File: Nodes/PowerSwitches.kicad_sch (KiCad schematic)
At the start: 46 parts, among them IC1 VNQ9080AJTR, IC2 VNQ9080AJTR, T21 Conn_01x01, T22 Conn_01x01

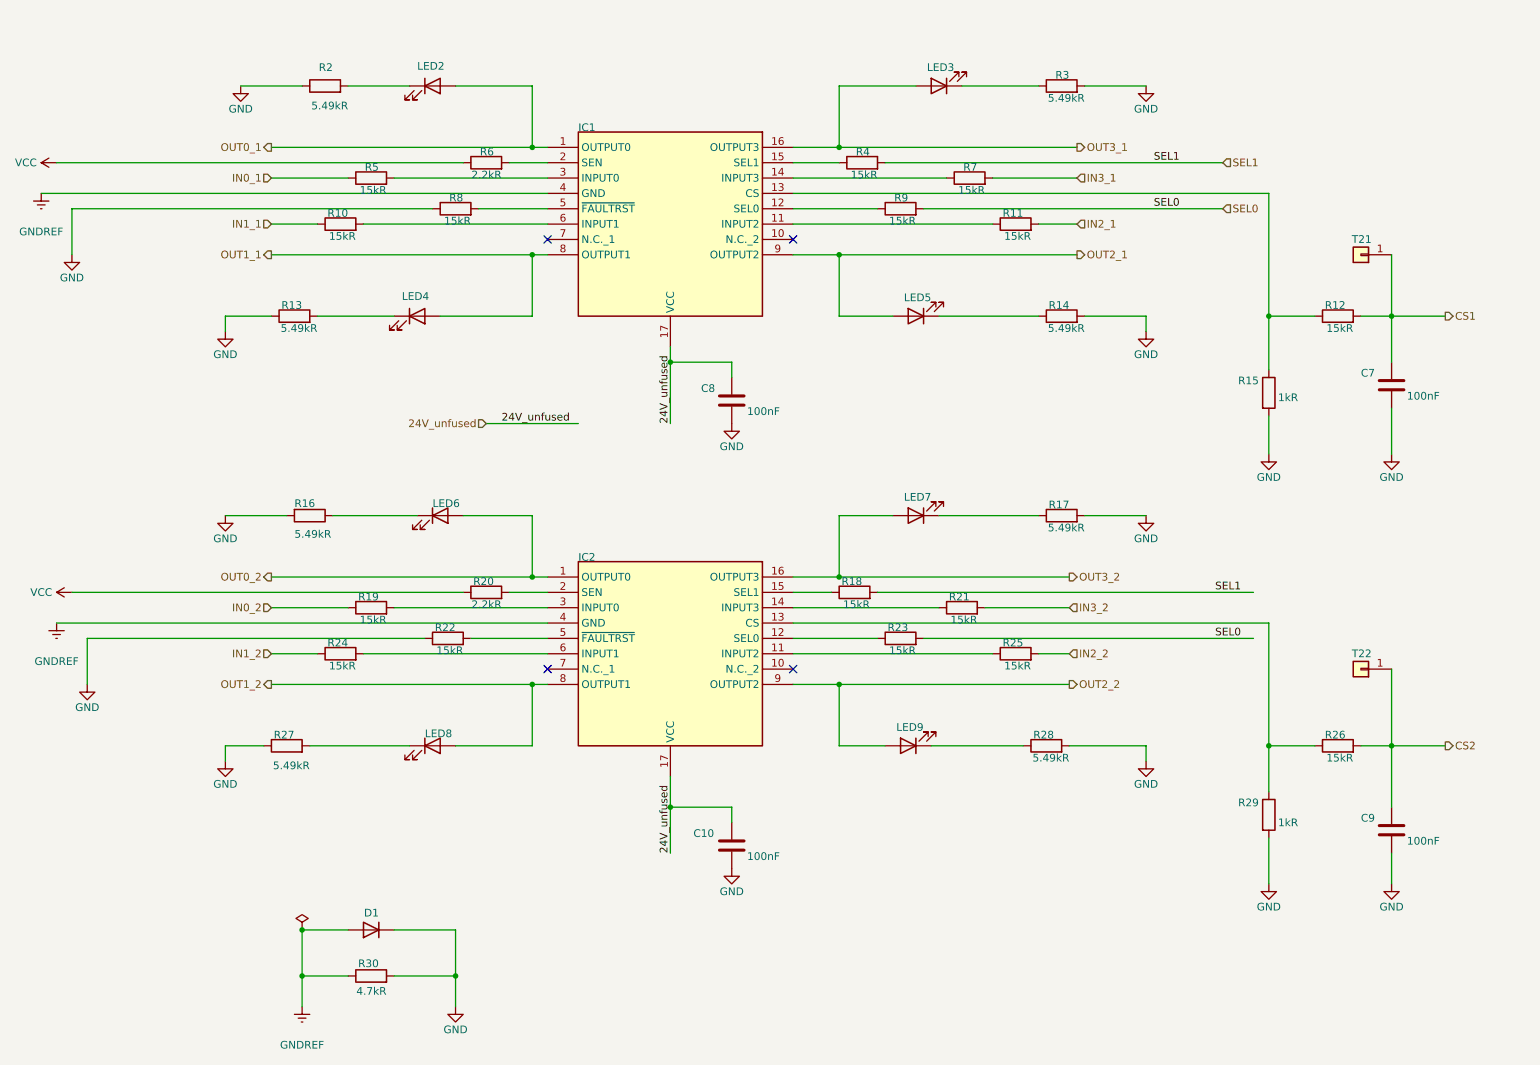
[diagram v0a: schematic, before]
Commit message: Nodes v2.1.2 Improved
- Improved schematic design
- Added two 4.7 uF caps according to the datasheets of the microchips
- Other small changes
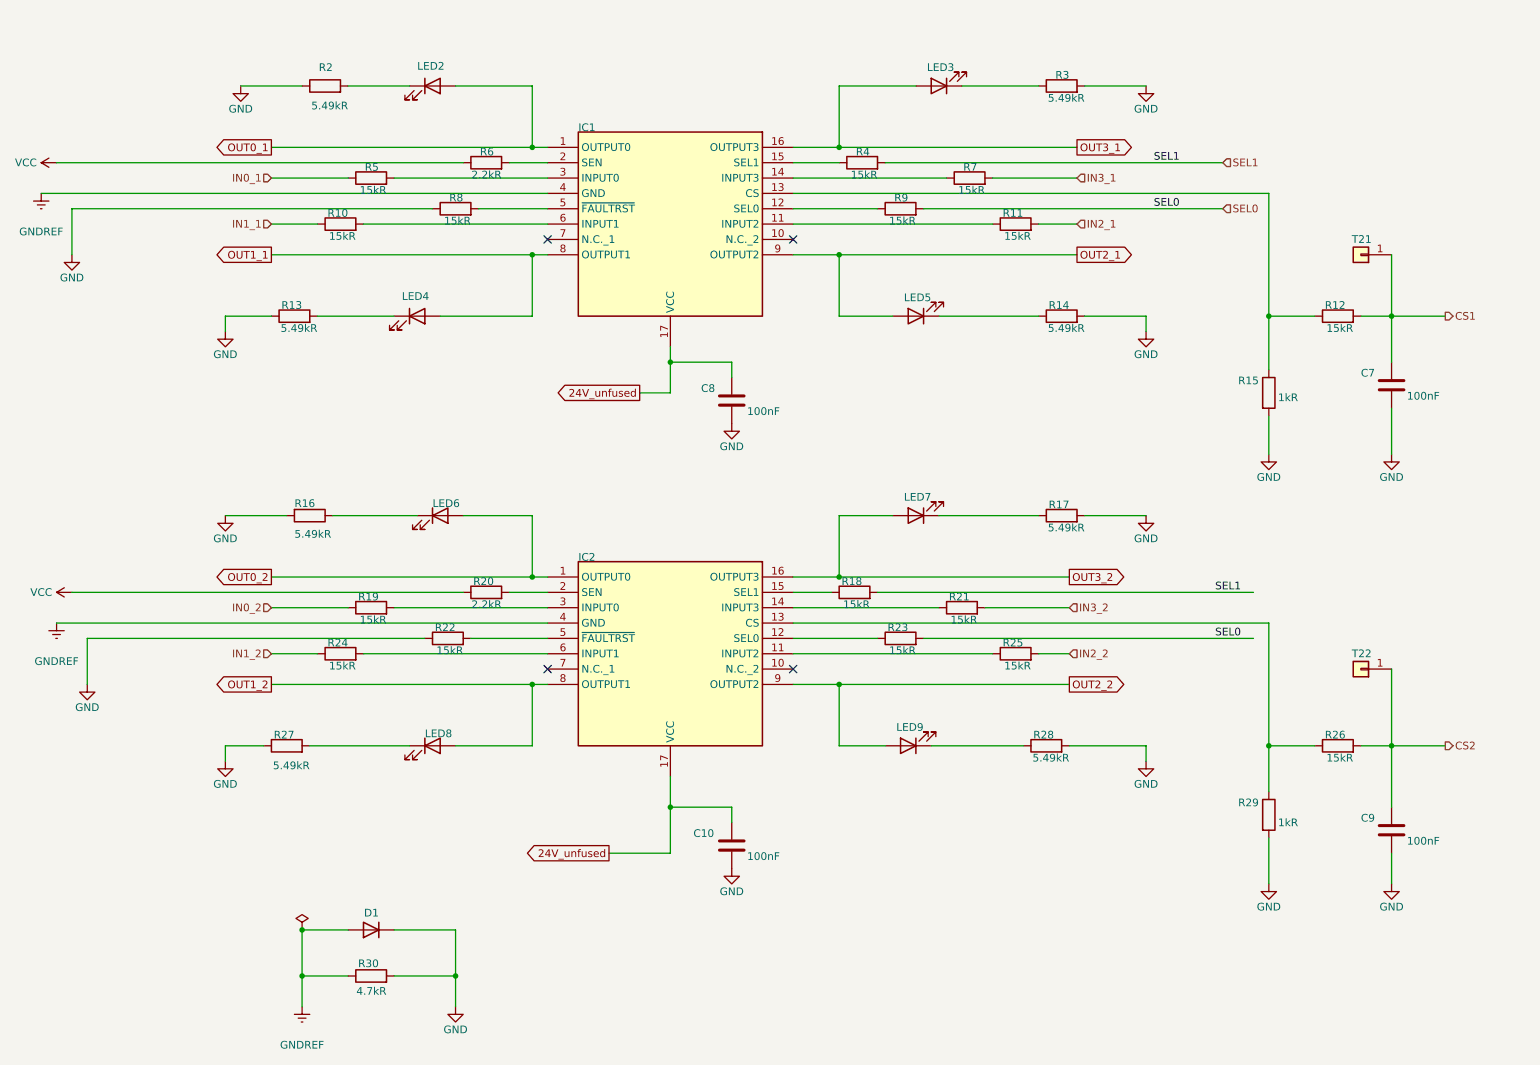
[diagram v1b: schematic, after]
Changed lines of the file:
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@@
+	(wire
+		(pts
+			(xy 125.73 77.47) (xy 120.65 77.47)
+		)
+		(stroke
+			(width 0.254)
+			(type default)
+		)
+	)
 	(wire
 		(pts
@@
 	(wire
 		(pts
-			(xy 125.73 72.39) (xy 125.73 82.55)
-		)
-		(stroke
-			(width 0.254)
-			(type default)
-		)
-	)
-	(wire
-		(pts
 			(xy 146.05 125.73) (xy 153.67 125.73)
 		)
@@
 	(wire
 		(pts
+			(xy 115.57 153.67) (xy 125.73 153.67)
+		)
+		(stroke
+			(width 0.254)
+			(type default)
+		)
+	)
+	(wire
+		(pts
 			(xy 102.87 64.77) (xy 102.87 54.61)
 		)
@@
 	(wire
 		(pts
-			(xy 95.25 82.55) (xy 110.49 82.55)
-		)
-		(stroke
-			(width 0.254)
-			(type default)
-		)
-	)
-	(wire
-		(pts
 			(xy 224.79 135.89) (xy 224.79 143.51)
 		)
@@
 		(pts
 			(xy 224.79 44.45) (xy 224.79 64.77)
+		)
+		(stroke
+			(width 0.254)
+			(type default)
+		)
+	)
+	(wire
+		(pts
+			(xy 125.73 72.39) (xy 125.73 77.47)
 		)
 		(stroke
@@
 		)
 	)
-	(label "24V_unfused"
-		(at 97.79 82.55 0)
-		(fields_autoplaced yes)
-		(effects
-			(font
-				(size 1.27 1.27)
-			)
-			(justify left bottom)
-		)
-	)
 	(label "SEL0"
 		(at 205.74 46.99 0)
@@
 		)
 	)
-	(label "24V_unfused"
-		(at 125.73 153.67 90)
-		(fields_autoplaced yes)
-		(effects
-			(font
-				(size 1.27 1.27)
-			)
-			(justify left bottom)
-		)
-	)
-	(label "24V_unfused"
-		(at 125.73 82.55 90)
-		(fields_autoplaced yes)
-		(effects
-			(font
-				(size 1.27 1.27)
-			)
-			(justify left bottom)
-		)
-	)
 	(label "SEL1"
 		(at 215.9 110.49 0)
@@
 		)
 	)
+	(global_label "OUT2_2"
+		(shape output)
+		(at 191.77 125.73 0)
+		(fields_autoplaced yes)
+		(effects
+			(font
+				(size 1.27 1.27)
+			)
+			(justify left)
+		)
+		(property "Intersheetrefs" "${INTERSHEET_REFS}"
+			(at 201.7704 125.73 0)
+			(effects
+				(font
+					(size 1.27 1.27)
+				)
+				(justify left)
+				(hide yes)
+			)
+		)
+	)
+	(global_label "OUT3_1"
+		(shape output)
+		(at 193.04 36.83 0)
+		(fields_autoplaced yes)
+		(effects
+			(font
+				(size 1.27 1.27)
+			)
+			(justify left)
+		)
+		(property "Intersheetrefs" "${INTERSHEET_REFS}"
+			(at 203.0404 36.83 0)
+			(effects
+				(font
+					(size 1.27 1.27)
+				)
+				(justify left)
+				(hide yes)
+			)
+		)
+	)
+	(global_label "OUT1_1"
+		(shape output)
+		(at 59.69 54.61 180)
+		(fields_autoplaced yes)
+		(effects
+			(font
+				(size 1.27 1.27)
+			)
+			(justify right)
+		)
+		(property "Intersheetrefs" "${INTERSHEET_REFS}"
+			(at 49.6896 54.61 0)
+			(effects
+				(font
+					(size 1.27 1.27)
+				)
+				(justify right)
+				(hide yes)
+			)
+		)
+	)
+	(global_label "OUT0_1"
+		(shape output)
+		(at 59.69 36.83 180)
+		(fields_autoplaced yes)
+		(effects
+			(font
+				(size 1.27 1.27)
+			)
+			(justify right)
+		)
+		(property "Intersheetrefs" "${INTERSHEET_REFS}"
+			(at 49.6896 36.83 0)
+			(effects
+				(font
+					(size 1.27 1.27)
+				)
+				(justify right)
+				(hide yes)
+			)
+		)
+	)
+	(global_label "OUT1_2"
+		(shape output)
+		(at 59.69 125.73 180)
+		(fields_autoplaced yes)
+		(effects
+			(font
+				(size 1.27 1.27)
+			)
+			(justify right)
+		)
+		(property "Intersheetrefs" "${INTERSHEET_REFS}"
+			(at 49.6896 125.73 0)
+			(effects
+				(font
+					(size 1.27 1.27)
+				)
+				(justify right)
+				(hide yes)
+			)
+		)
+	)
+	(global_label "24V_unfused"
+		(shape output)
+		(at 115.57 153.67 180)
+		(fields_autoplaced yes)
+		(effects
+			(font
+				(size 1.27 1.27)
+			)
+			(justify right)
+		)
+		(property "Intersheetrefs" "${INTERSHEET_REFS}"
+			(at 100.6712 153.67 0)
+			(effects
+				(font
+					(size 1.27 1.27)
+				)
+				(justify right)
+				(hide yes)
+			)
+		)
+	)
+	(global_label "OUT2_1"
+		(shape output)
+		(at 193.04 54.61 0)
+		(fields_autoplaced yes)
+		(effects
+			(font
+				(size 1.27 1.27)
+			)
+			(justify left)
+		)
+		(property "Intersheetrefs" "${INTERSHEET_REFS}"
+			(at 203.0404 54.61 0)
+			(effects
+				(font
+					(size 1.27 1.27)
+				)
+				(justify left)
+				(hide yes)
+			)
+		)
+	)
+	(global_label "24V_unfused"
+		(shape output)
+		(at 120.65 77.47 180)
+		(fields_autoplaced yes)
+		(effects
+			(font
+				(size 1.27 1.27)
+			)
+			(justify right)
+		)
+		(property "Intersheetrefs" "${INTERSHEET_REFS}"
+			(at 105.7512 77.47 0)
+			(effects
+				(font
+					(size 1.27 1.27)
+				)
+				(justify right)
+				(hide yes)
+			)
+		)
+	)
+	(global_label "OUT0_2"
+		(shape output)
+		(at 59.69 107.95 180)
+		(fields_autoplaced yes)
+		(effects
+			(font
+				(size 1.27 1.27)
+			)
+			(justify right)
+		)
+		(property "Intersheetrefs" "${INTERSHEET_REFS}"
+			(at 49.6896 107.95 0)
+			(effects
+				(font
+					(size 1.27 1.27)
+				)
+				(justify right)
+				(hide yes)
+			)
+		)
+	)
+	(global_label "OUT3_2"
+		(shape output)
+		(at 191.77 107.95 0)
+		(fields_autoplaced yes)
+		(effects
+			(font
+				(size 1.27 1.27)
+			)
+			(justify left)
+		)
+		(property "Intersheetrefs" "${INTERSHEET_REFS}"
+			(at 201.7704 107.95 0)
+			(effects
+				(font
+					(size 1.27 1.27)
+				)
+				(justify left)
+				(hide yes)
+			)
+		)
+	)
 	(hierarchical_label "SEL0"
 		(shape input)
@@
 		)
 	)
-	(hierarchical_label "OUT3_1"
-		(shape output)
-		(at 193.04 36.83 0)
-		(fields_autoplaced yes)
-		(effects
-			(font
-				(size 1.27 1.27)
-			)
-			(justify left)
-		)
-	)
 	(hierarchical_label "CS1"
 		(shape output)
@@
 		)
 	)
-	(hierarchical_label "OUT1_1"
-		(shape output)
-		(at 59.69 54.61 180)
-		(fields_autoplaced yes)
-		(effects
-			(font
-				(size 1.27 1.27)
-			)
-			(justify right)
-		)
-	)
 	(hierarchical_label "IN2_1"
 		(shape input)
@@
 		)
 	)
-	(hierarchical_label "OUT1_2"
-		(shape output)
-		(at 59.69 125.73 180)
-		(fields_autoplaced yes)
-		(effects
-			(font
-				(size 1.27 1.27)
-			)
-			(justify right)
-		)
-	)
 	(hierarchical_label "IN0_2"
 		(shape input)
@@
 		)
 	)
-	(hierarchical_label "OUT0_2"
-		(shape output)
-		(at 59.69 107.95 180)
-		(fields_autoplaced yes)
-		(effects
-			(font
-				(size 1.27 1.27)
-			)
-			(justify right)
-		)
-	)
-	(hierarchical_label "OUT2_1"
-		(shape output)
-		(at 193.04 54.61 0)
-		(fields_autoplaced yes)
-		(effects
-			(font
-				(size 1.27 1.27)
-			)
-			(justify left)
-		)
-	)
-	(hierarchical_label "24V_unfused"
-		(shape input)
-		(at 95.25 82.55 180)
-		(fields_autoplaced yes)
-		(effects
-			(font
-				(size 1.27 1.27)
-			)
-			(justify right)
-		)
-	)
-	(hierarchical_label "OUT2_2"
-		(shape output)
-		(at 191.77 125.73 0)
-		(fields_autoplaced yes)
-		(effects
-			(font
-				(size 1.27 1.27)
-			)
-			(justify left)
-		)
-	)
 	(hierarchical_label "IN1_2"
 		(shape input)
@@
 		)
 	)
-	(hierarchical_label "OUT0_1"
-		(shape output)
-		(at 59.69 36.83 180)
-		(fields_autoplaced yes)
-		(effects
-			(font
-				(size 1.27 1.27)
-			)
-			(justify right)
-		)
-	)
 	(hierarchical_label "IN0_1"
 		(shape input)
@@
 		(fields_autoplaced yes)
 		(effects
-			(font
-				(size 1.27 1.27)
-			)
-			(justify left)
-		)
-	)
-	(hierarchical_label "OUT3_2"
-		(shape output)
-		(at 191.77 107.95 0)
-		(fields_autoplaced yes)
-		(effects

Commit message: Nodes v2.2
- This version not compatible with BOB v.2.1.2 and older!
- Completely new layout design
- New power supply system with new voltage regulators
- New microchip STM32G431RBTx for the Analog Node
- New connection system (instead of 18 pin headers now 8 pin and pins were grouped by functions)
- Reduced size of the board by 5%
- Removed power switch for the Analog Node (because this functionality is now provided by a separate voltage regulator. for a more stable voltage)
- Removable ground from the holes added
- Layer numbers added
- Small improvements of the components information were made
- New oscillator for the Nodes
- Removed CAN1, so now only one CAN connection due to the capabilities of the new microchip
- Other small changes and fixes on the schematic and design
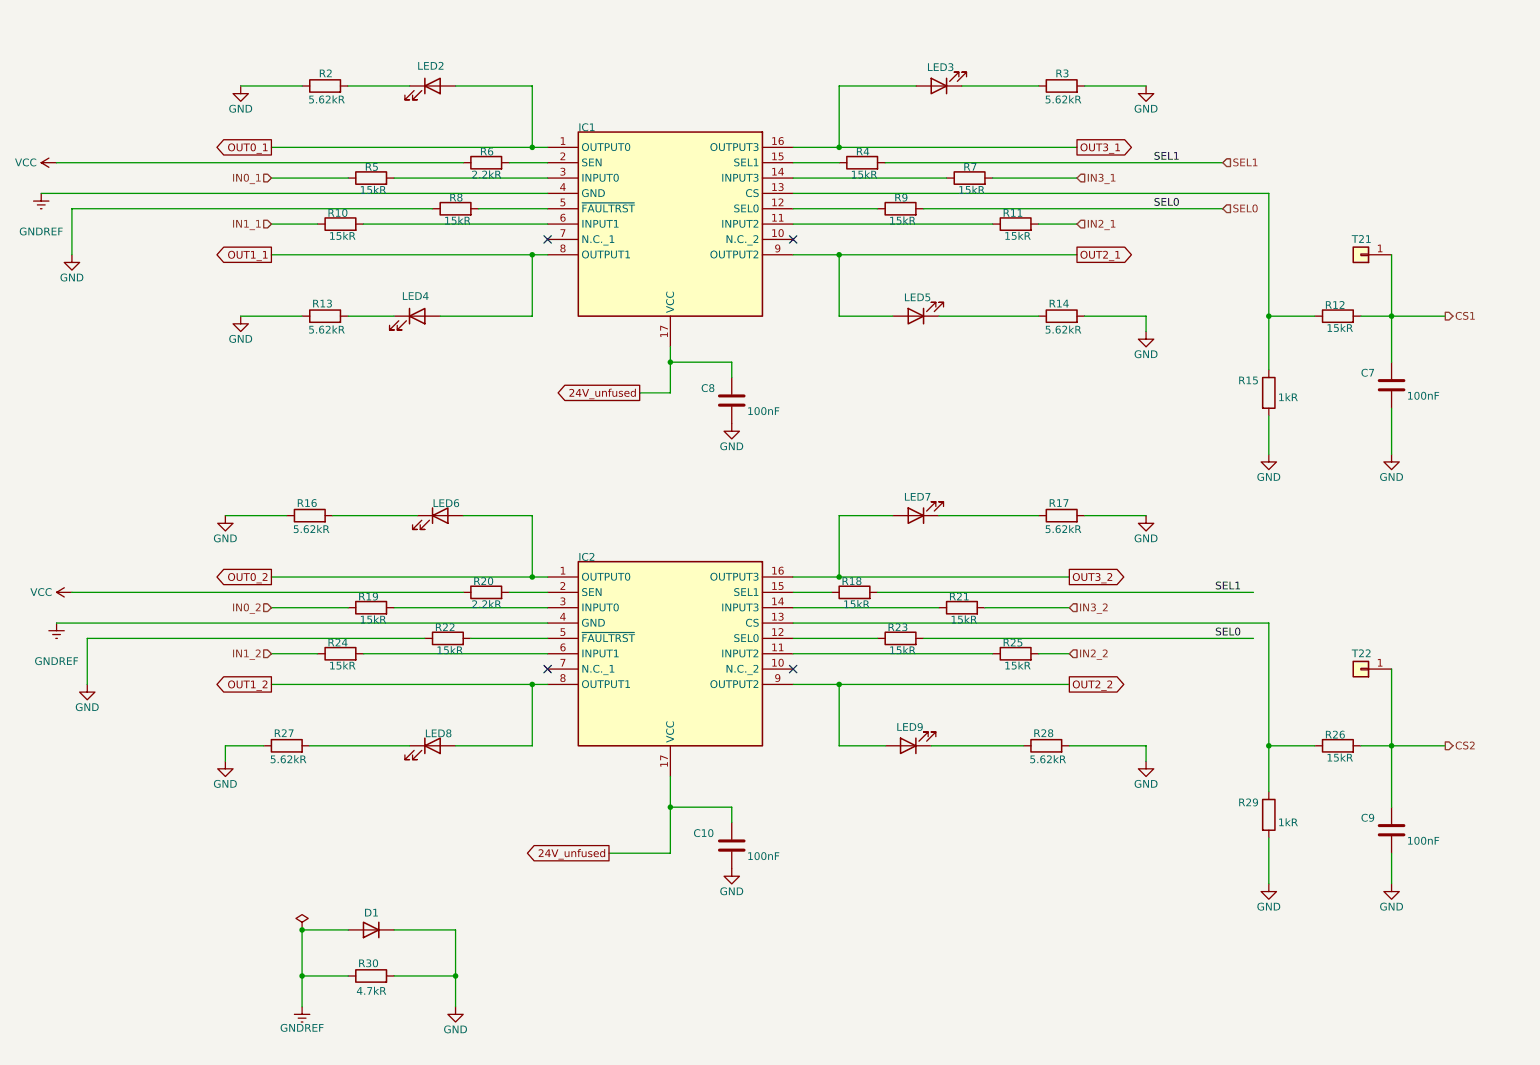
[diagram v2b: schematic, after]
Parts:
- R13, R14, R16, R17, R2, R27, R28, R3: value 5.49kR -> 5.62kR; ALTIUM_VALUE 5.49kR -> (none); AUTOMOTIVE Yes -> (none); AUTOMOTIVE GRADE Grade 0 -> (none); CATEGORY Res -> (none); COMPONENTLINK2DESCRIPTION Datasheet -> (none); COMPONENTLINK2URL http://www.yageo.com/documents/recent/PYu-AC_51_RoHS_L_6.pdf -> (none); COMPOSITION Thick Film -> (none); DEVICE CLASS L1 Passive Components -> (none); DEVICE CLASS L2 Resistors -> (none); DEVICE CLASS L3 Chip SMD Resistors -> (none); DIGIKEY DESCRIPTION Res SMD 5.49K Ohm 1% 1/8W 0805 -> (none); FOOTPRINT URL http://www.yageo.com/exep/pages/download/literatures/PYu-R_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 -> (none); HEIGHT 0.6mm -> (none); IPC LAND PATTERN NAME RESC200125X50 -> (none); LEAD FREE Yes -> (none); MANUFACTURER Yageo -> (none); MANUFACTURER PART NUMBER AC0805FR-075K49L -> (none); OCTOPART https://octopart.com/ac0805fr-075k49l-yageo-71367778 -> (none); PACKAGE AC0805 -> (none); POWER RATING 1/8W -> (none); RESISTANCE 5.49KΩ -> (none); ROHS TRUE -> (none); SERIES AC -> (none); TEMPERATURE -55°C to +155°C -> (none); TEMPERATURE RANGE HIGH +155°C -> (none); TEMPERATURE RANGE LOW -55°C -> (none); TOLERANCE 0.01 -> (none); VOLTAGE RATING 150V -> (none)
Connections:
- net GND: now also R16.1; no longer R16.2
- net at LED6.1 (K): now also R16.2; no longer R16.1

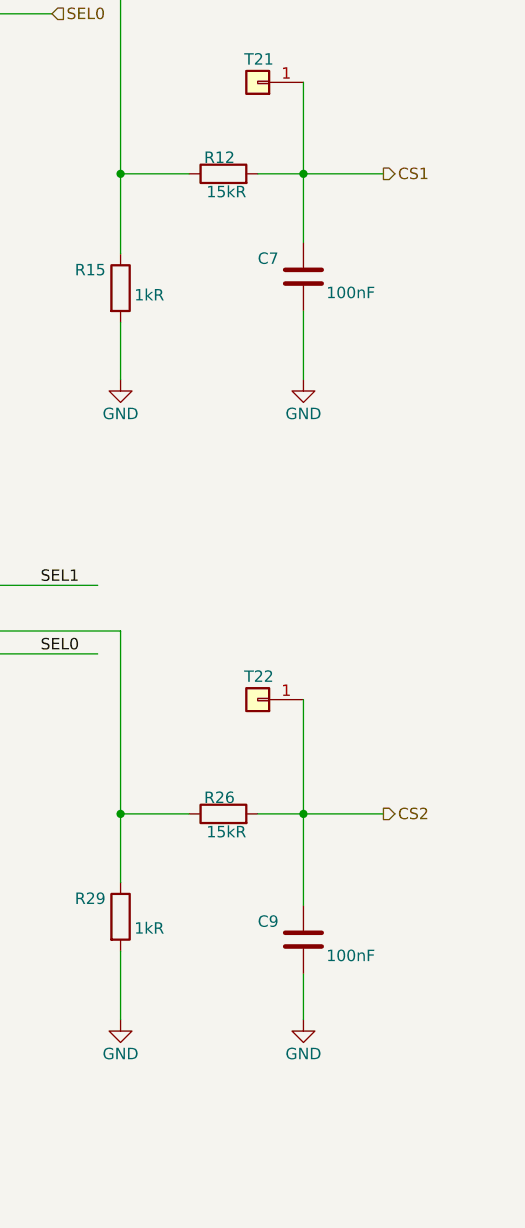
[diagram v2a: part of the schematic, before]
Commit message: Nodes v2.2.4
- Added two Zener Diodes for CS pins of High-Side drivers
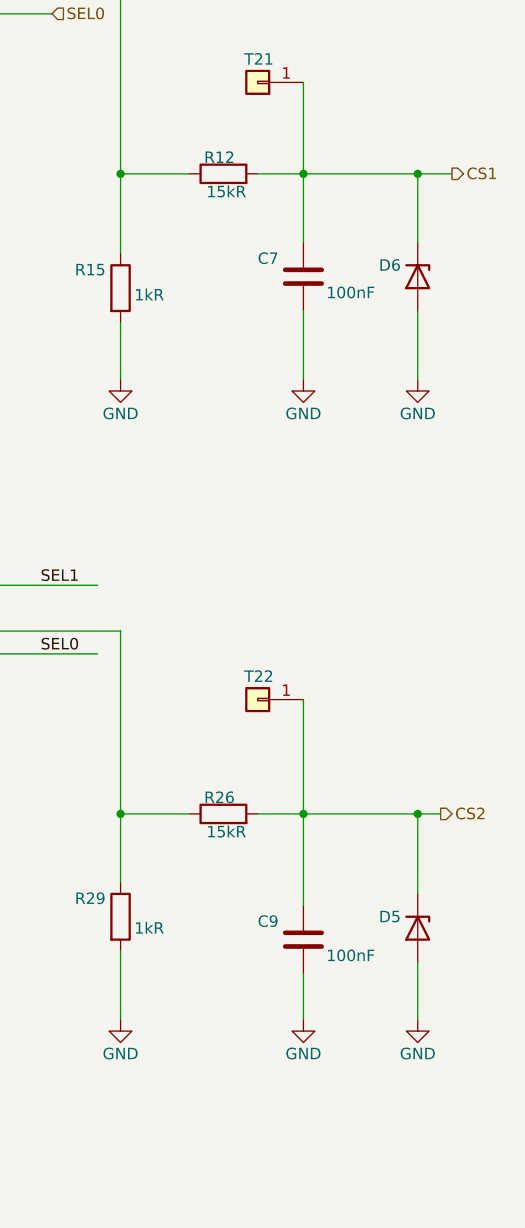
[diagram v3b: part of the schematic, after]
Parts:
- added D5, D6: 1SMA5913BT3G, Diode_SMD:D_SMA_Handsoldering, symbol Device:D_Zener
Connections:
- net CS1: now also D6.1 (K)
- net CS2: now also D5.1 (K)
- net GND: now also D5.2 (A), D6.2 (A)
